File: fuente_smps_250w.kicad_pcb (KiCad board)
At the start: 2 copper layers, 160 x 60 mm, 53 parts, among them J1 Conn_01x03, J2 Conn_01x03, Q1 2N3904, Q2 2N3906, Q3 2N3904, Q4 2N3906, Q5 IRFZ44N, Q6 IRFZ44N, Q7 IRFZ44N, Q8 IRFZ44N, U1 SG3525A, U2 LTV-817S-TA1

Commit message: terminando la  version con sg3525a
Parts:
- moved R13 1.91 mm to (129.6, 70.3)
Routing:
- net Net-(R14-Pad2): track 51.4 -> 63.6 mm, vias 2 -> 0
- net /Filtro/T_B: track 78.8 -> 68.8 mm
- net Net-(D3-Pad2): track 22.7 -> 14.0 mm
- net /OSC_SG3525/VREF: track 62.0 -> 64.9 mm
- net /OSC_SG3525/Sense: track 143.5 -> 141.6 mm
- net /Filtro/T_A: track 72.2 -> 70.8 mm
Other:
- outline, holes or cut-outs redrawn
- board text added: "SG3525A"

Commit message: terminando el diseno
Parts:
- removed the C12 at (195.3, 97.7)
- removed C14: 1000uF, Capacitor_THT:CP_Radial_D10.0mm_P5.00mm
- removed C16: 0.1uF, Capacitor_THT:C_Disc_D3.8mm_W2.6mm_P2.50mm
- removed U2: LTV-817S-TA1, Package_DIP:DIP-4_W7.62mm_LongPads
- added IC1: TL494, Package_DIP:DIP-16_W7.62mm_LongPads, F.Cu at (92.7, 85.2)
- added R15: 270, Resistor_THT:R_Axial_DIN0309_L9.0mm_D3.2mm_P15.24mm_Horizontal, F.Cu at (105.5, 109.0)
- C1: value 15nF -> 2.5uF; footprint Capacitor_THT:C_Disc_D9.0mm_W2.5mm_P5.00mm -> Capacitor_THT:CP_Radial_D4.0mm_P2.00mm
- C13: value 1000uF -> 0.1uF; footprint Capacitor_THT:CP_Radial_D10.0mm_P5.00mm -> Capacitor_THT:C_Disc_D3.8mm_W2.6mm_P2.50mm
- C2: value 0.1uF -> 1nF; footprint Capacitor_THT:C_Disc_D3.8mm_W2.6mm_P2.50mm -> Capacitor_THT:C_Disc_D4.3mm_W1.9mm_P5.00mm
- C3: value 0.1uF -> 0.33uF; footprint Capacitor_THT:C_Disc_D3.8mm_W2.6mm_P2.50mm -> Capacitor_THT:C_Disc_D4.3mm_W1.9mm_P5.00mm
- C4, C5: value 0.1uF -> 1000uF; footprint Capacitor_THT:C_Disc_D3.8mm_W2.6mm_P2.50mm -> Capacitor_THT:CP_Radial_D10.0mm_P5.00mm
- C6: value 0.33uF -> 1000uF; footprint Capacitor_THT:C_Disc_D4.3mm_W1.9mm_P5.00mm -> Capacitor_THT:CP_Radial_D10.0mm_P5.00mm
- D1: value MBRF1080CTR -> D_Zener_ALT; footprint Package_TO_SOT_THT:TO-220-3_Vertical -> Diode_THT:D_A-405_P10.16mm_Horizontal
- D2: value MBRF1080CT -> D_Zener_ALT; footprint Package_TO_SOT_THT:TO-220-3_Vertical -> Diode_THT:D_A-405_P10.16mm_Horizontal
- D3: value D_Zener_ALT -> MBRF1080CTR; footprint Diode_THT:D_A-405_P10.16mm_Horizontal -> Package_TO_SOT_THT:TO-220-3_Vertical
- D4: value D_Zener_ALT -> MBRF1080CT; footprint Diode_THT:D_A-405_P10.16mm_Horizontal -> Package_TO_SOT_THT:TO-220-3_Vertical
- R1: value 4.7K -> 1K
- R10, R9: value 10 -> 1K
- R12: value 270 -> 10; footprint Resistor_THT:R_Axial_DIN0309_L9.0mm_D3.2mm_P15.24mm_Horizontal -> Resistor_THT:R_Axial_DIN0207_L6.3mm_D2.5mm_P10.16mm_Horizontal
- R13: value 1K -> 10
- R14: value 510 -> 10
- R2: value 4.7K -> 510
- R3: value 4.7K -> 9.1K
- R4: value 33 -> 1K
- R5: value 820 -> 510
- R6: value 1K -> 51K
- R7: value 1K -> 50K
- R8: value 10 -> 10K
- U1: value SG3525A -> LTV-817S-TA1; footprint Package_DIP:DIP-16_W7.62mm_LongPads -> Package_DIP:DIP-4_W7.62mm_LongPads
- moved C5 112.2 mm to (195.5, 75.5), turned to 270 degrees
- moved C4 105.1 mm to (195.5, 102.5), turned to 90 degrees
- moved R14 88.9 mm to (92.5, 72.5), turned to 0 degrees
- moved R2 77.0 mm to (179.5, 83.5)
- moved C6 63.7 mm to (184.3, 102.5)
- moved U1 56.9 mm to (151.1, 73.0), turned to 180 degrees
- moved R11 54.1 mm to (125.0, 117.5), turned to 180 degrees
- moved D1 49.0 mm to (178.0, 72.5)
- moved R8 36.2 mm to (104.0, 87.5), turned to 270 degrees
- moved D4 35.8 mm to (175.5, 121.5), turned to 180 degrees
- moved D2 34.2 mm to (176.5, 102.5), turned to 90 degrees
- moved R6 33.8 mm to (79.5, 89.0), turned to 0 degrees
- moved C3 32.5 mm to (123.0, 83.8)
- moved R1 29.6 mm to (130.0, 70.5), turned to 0 degrees
- moved R10 28.0 mm to (107.5, 97.5), turned to 90 degrees
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- renumbered C15 to C12
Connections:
- C1 pad 1: Net-(C1-Pad1) -> VREF
- C1 pad 2: GND -> Net-(C1-Pad2)
- C10 pad 1: GNDREF -> /Filtro/VCC
- C10 pad 2: /Filtro/-VCC -> GNDREF
- C11 pad 1: /Filtro/VCC -> GNDREF
- C11 pad 2: GNDREF -> /Filtro/-VCC
- C13 pad 1: /Filtro/VCC -> GNDREF
- C13 pad 2: GNDREF -> /Filtro/-VCC
- C2 pad 1: /OSC_SG3525/VREF -> Net-(C2-Pad1)
- C3 pad 2: GND -> Net-(C3-Pad2)
- C4 pad 1: GND -> /Filtro/VCC
- C4 pad 2: Net-(C4-Pad2) -> GNDREF
- C5 pad 1: GND -> GNDREF
- C5 pad 2: Net-(C5-Pad2) -> /Filtro/-VCC
- C6 pad 1: Net-(C6-Pad1) -> /Filtro/VCC
- C6 pad 2: Net-(C6-Pad2) -> GNDREF
- C7 pad 1: /Filtro/VCC -> GNDREF
- C7 pad 2: GNDREF -> /Filtro/-VCC
- C8 pad 1: GNDREF -> /Filtro/VCC
- C8 pad 2: /Filtro/-VCC -> GNDREF
- C9 pad 1: /Filtro/VCC -> GNDREF
- C9 pad 2: GNDREF -> /Filtro/-VCC
- D1 pad 1: /Filtro/T_A -> Net-(D1-Pad1)
- D1 pad 2: /Filtro/-VCC -> Net-(D1-Pad2)
- D2 pad 1: /Filtro/T_B -> /Filtro/VCC
- D2 pad 2: /Filtro/VCC -> Net-(D1-Pad1)
- D3 pad 1: Net-(D3-Pad1) -> /Filtro/T_A
- D3 pad 2: Net-(D3-Pad2) -> /Filtro/-VCC
- D4 pad 1: /Filtro/VCC -> /Filtro/T_B
- D4 pad 2: Net-(D3-Pad1) -> /Filtro/VCC
- H1 pad 1: GND -> Net-(H1-Pad1)
- H2 pad 1: GND -> Net-(H2-Pad1)
- H3 pad 1: GNDREF -> Net-(H3-Pad1)
- H4 pad 1: GNDREF -> Net-(H4-Pad1)
- J1 pad 2: /OSC_SG3525/shutdown -> (no net)
- Q6 pad 2: Net-(C6-Pad2) -> Net-(C3-Pad2)
- Q8 pad 2: Net-(C6-Pad2) -> Net-(C3-Pad2)
- R1 pad 1: /OSC_SG3525/VREF -> GND
- R1 pad 2: Net-(R1-Pad2) -> /OSC_TL494/Sense
- R10 pad 1: Net-(Q6-Pad1) -> /transformacion/In_B
- R10 pad 2: Net-(Q3-Pad1) -> GND
- R11 pad 1: Net-(Q8-Pad1) -> Net-(Q7-Pad1)
- R11 pad 2: Net-(Q3-Pad1) -> Net-(Q1-Pad1)
- R12 pad 1: Net-(Q5-Pad2) -> Net-(Q5-Pad1)
- R12 pad 2: Net-(C6-Pad1) -> Net-(Q1-Pad1)
- R13 pad 1: GND -> Net-(Q6-Pad1)
- R13 pad 2: /OSC_SG3525/Sense -> Net-(Q3-Pad1)
- R14 pad 1: /Filtro/-VCC -> Net-(Q8-Pad1)
- R14 pad 2: Net-(R14-Pad2) -> Net-(Q3-Pad1)
- R2 pad 1: GND -> /Filtro/-VCC
- R2 pad 2: Net-(R1-Pad2) -> Net-(R2-Pad2)
- R3 pad 1: Net-(R3-Pad1) -> VREF
- R3 pad 2: GND -> Net-(C1-Pad2)
- R4 pad 1: Net-(R4-Pad1) -> Net-(C1-Pad2)
- R4 pad 2: Net-(C1-Pad1) -> GND
- R5 pad 1: Net-(C5-Pad2) -> Net-(IC1-Pad2)
- R5 pad 2: Net-(R5-Pad2) -> VREF
- R6 pad 1: /transformacion/In_A -> Net-(IC1-Pad2)
- R6 pad 2: GND -> Net-(IC1-Pad3)
- R7 pad 1: /transformacion/In_B -> Net-(IC1-Pad6)
- R8 pad 1: Net-(Q7-Pad1) -> +12V
- R8 pad 2: Net-(Q1-Pad1) -> Net-(IC1-Pad11)
- R9 pad 1: Net-(Q5-Pad1) -> /transformacion/In_A
- R9 pad 2: Net-(Q1-Pad1) -> GND
- RV1 pad 2: Net-(R14-Pad2) -> Net-(R2-Pad2)
- RV1 pad 3: Net-(R14-Pad2) -> Net-(R2-Pad2)
- TR1 pad 1: Net-(C6-Pad2) -> Net-(C3-Pad2)
- U1 pad 1: /OSC_SG3525/Sense -> Net-(D1-Pad2)
- U1 pad 2: Net-(R1-Pad2) -> Net-(RV1-Pad1)
- U1 pad 3: Net-(C3-Pad1) -> /OSC_TL494/Sense
- U1 pad 4: Net-(U1-Pad4) -> (no net)
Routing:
- net /OSC_SG3525/Sense: track 141.6 -> 0.00 mm, vias 2 -> 0
- net GND: track 95.8 -> 0.00 mm
- net Net-(C6-Pad2): track 79.7 -> 0.00 mm
- net VREF: track 0.00 -> 73.0 mm
- net GNDREF: track 139.5 -> 66.9 mm
- net /OSC_TL494/Sense: track 0.00 -> 68.1 mm, vias 0 -> 2
- net /OSC_SG3525/VREF: track 64.9 -> 0.00 mm, vias 2 -> 0
- net Net-(R14-Pad2): track 63.6 -> 0.00 mm
- net +12V: track 83.0 -> 140.6 mm, vias 0 -> 2
- net Net-(C3-Pad2): track 0.00 -> 55.7 mm
- net /OSC_SG3525/shutdown: track 49.6 -> 0.00 mm
- net Net-(R2-Pad2): track 0.00 -> 35.9 mm, vias 0 -> 2
- net Net-(C1-Pad2): track 0.00 -> 26.3 mm
- net Net-(C3-Pad1): track 4.44 -> 30.6 mm
- net Net-(D1-Pad2): track 0.00 -> 26.0 mm
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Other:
- board size 160 x 60 mm -> 156.5 x 60 mm
- board text added: "TL494"
- board text removed: "SG3525A"

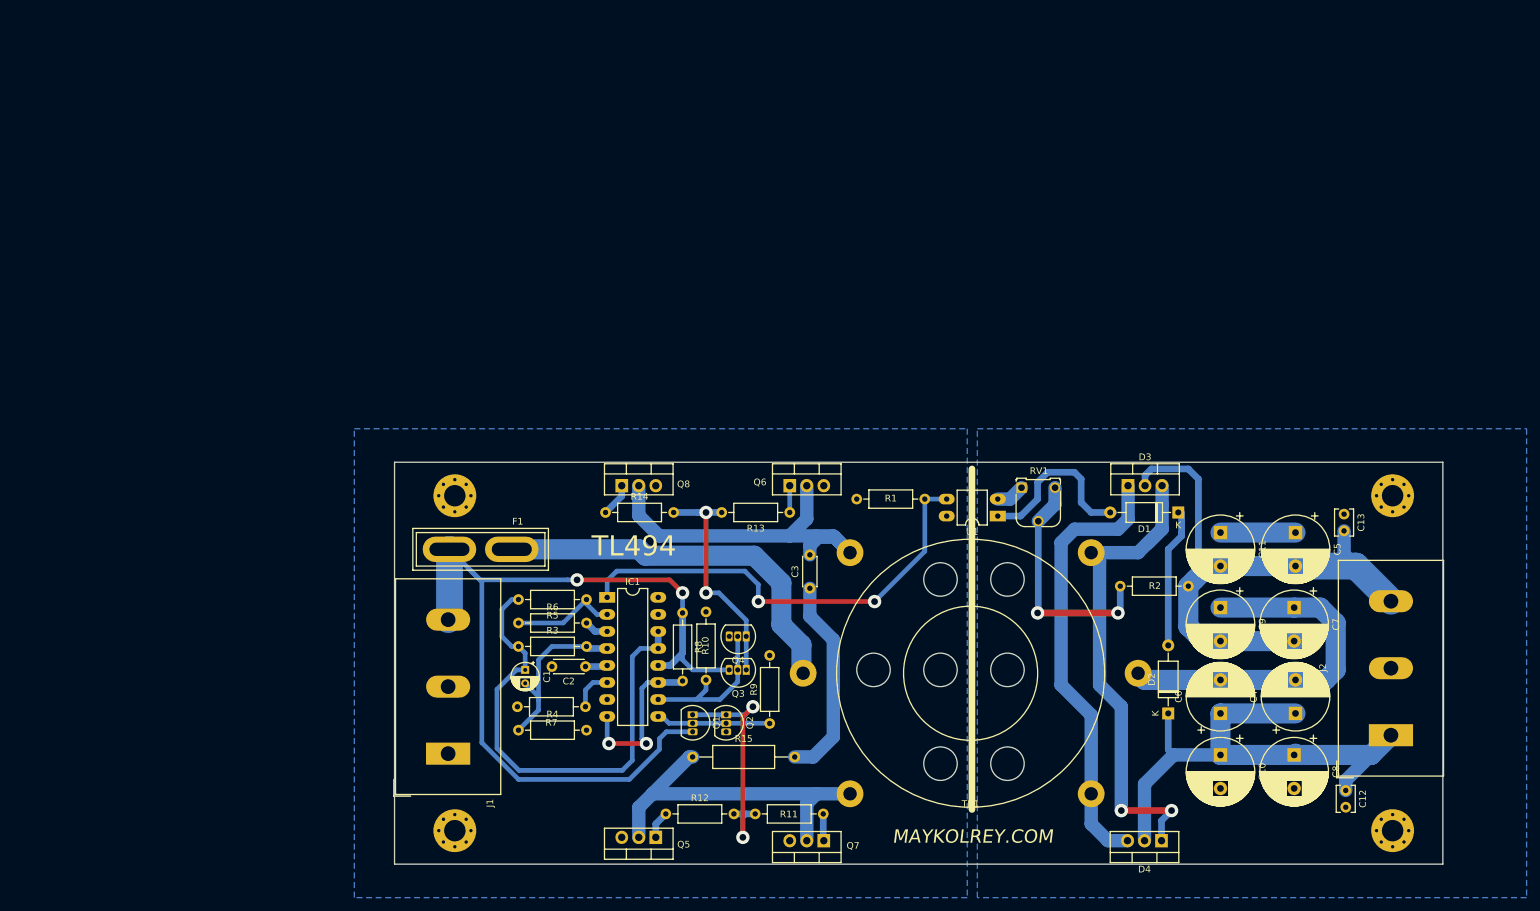
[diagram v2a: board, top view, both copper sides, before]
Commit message: separando el modulo de oscilacion en otra  placa
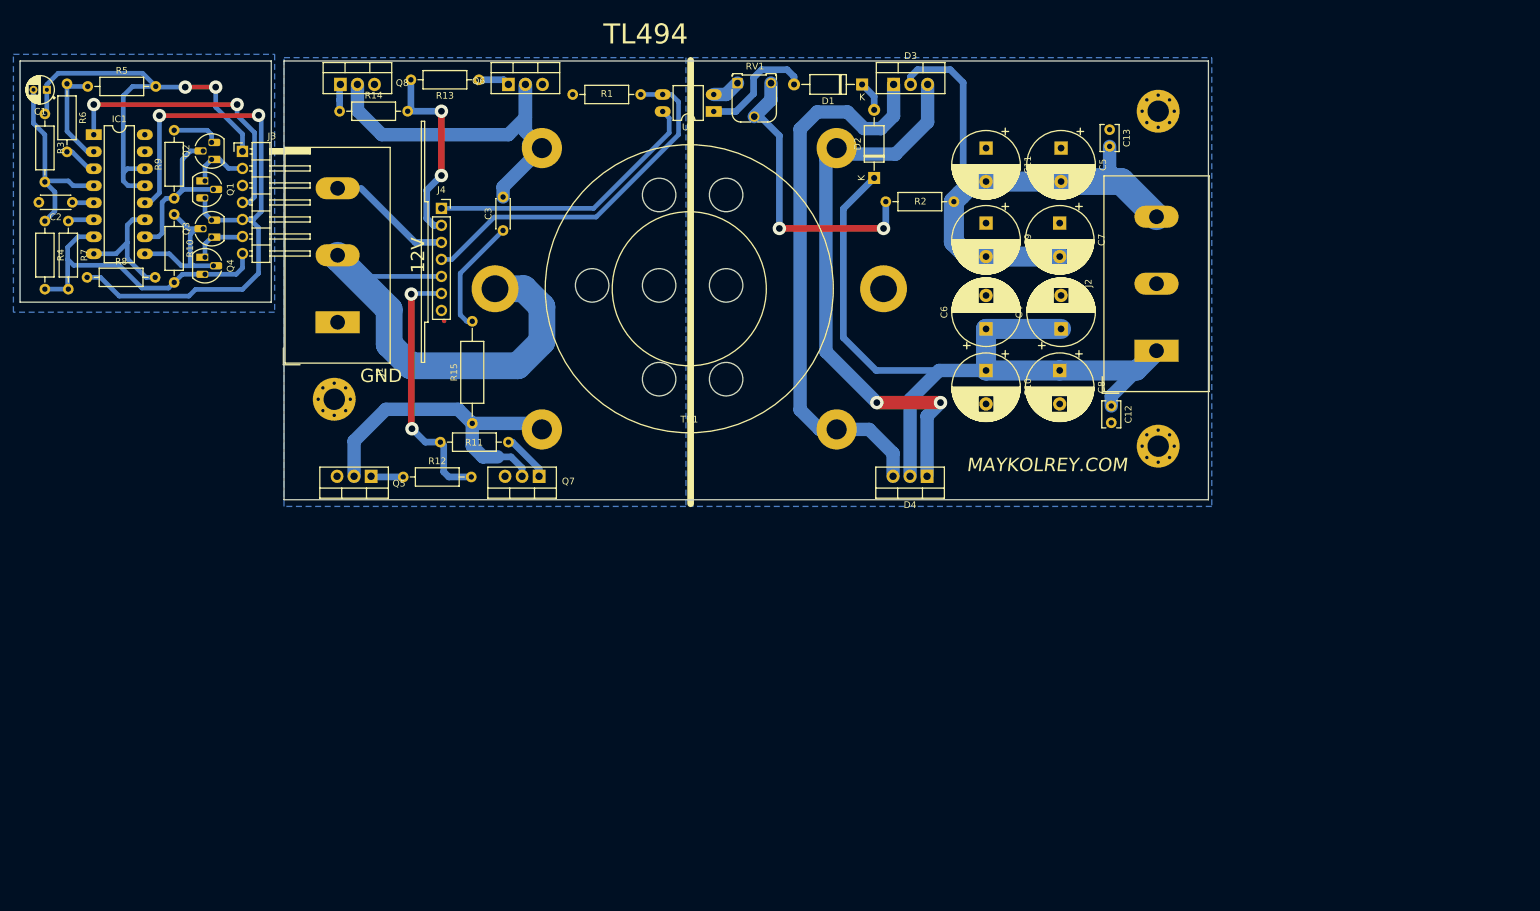
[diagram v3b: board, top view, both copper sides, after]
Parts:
- removed F1: Fuse, Fuse:Fuse_Blade_ATO_directSolder
- removed H2: MountingHole_Pad, MountingHole:MountingHole_3.2mm_M3_Pad_Via
- added J3: Conn_01x03, Connector_PinHeader_2.54mm:PinHeader_1x07_P2.54mm_Horizontal, F.Cu at (38.3, 18.6)
- added J4: Conn_01x03, Connector_PinSocket_2.54mm:PinSocket_1x07_P2.54mm_Vertical, F.Cu at (68.0, 27.1)
- Q1, Q2, Q3, Q4: footprint Package_TO_SOT_THT:TO-92L_Inline -> Package_TO_SOT_THT:TO-92L_HandSolder
- moved R9 118.5 mm to (28.1, 25.6)
- moved Q2 113.0 mm to (33.7, 19.8), turned to 90 degrees
- moved C1 112.2 mm to (9.10, 9.40), turned to 180 degrees
- moved Q1 107.9 mm to (32.7, 23.0)
- moved R5 106.8 mm to (15.2, 8.90), turned to 0 degrees
- moved R3 106.4 mm to (8.80, 13.0), turned to 270 degrees
- moved R7 105.9 mm to (12.3, 29.0), turned to 270 degrees
- moved R10 105.5 mm to (28.1, 28.0), turned to 270 degrees
- moved R6 105.0 mm to (12.1, 8.50), turned to 270 degrees
- moved R4 103.8 mm to (8.80, 29.0), turned to 270 degrees
- moved C2 103.3 mm to (12.9, 26.2)
- moved IC1 103.2 mm to (16.1, 16.1)
- moved Q3 102.7 mm to (33.7, 31.4), turned to 90 degrees
- moved R8 102.0 mm to (15.1, 37.4), turned to 0 degrees
- moved Q4 98.7 mm to (32.7, 34.4), turned to 270 degrees
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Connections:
- net VREF renamed /OSC_TL494/VREF
- C2 pad 2: GND -> GNDA
- IC1 pad 10: /transformacion/In_B -> /OSC_TL494/E2
- IC1 pad 12: +12V -> +12VA
- IC1 pad 7: GND -> GNDA
- IC1 pad 9: /transformacion/In_A -> /OSC_TL494/E1
- J1 pad 2: (no net) -> +12V
- J1 pad 3: +12V -> /shut_in
- Q1 pad 1: Net-(Q1-Pad1) -> /OSC_TL494/Out_B
- Q1 pad 2: /transformacion/In_A -> /OSC_TL494/E2
- Q1 pad 3: +12V -> +12VA
- Q2 pad 1: Net-(Q1-Pad1) -> /OSC_TL494/Out_B
- Q2 pad 2: /transformacion/In_A -> /OSC_TL494/E2
- Q2 pad 3: GND -> GNDA
- Q3 pad 1: Net-(Q3-Pad1) -> /OSC_TL494/Out_A
- Q3 pad 2: /transformacion/In_B -> /OSC_TL494/E1
- Q3 pad 3: +12V -> +12VA
- Q4 pad 1: Net-(Q3-Pad1) -> /OSC_TL494/Out_A
- Q4 pad 2: /transformacion/In_B -> /OSC_TL494/E1
- Q4 pad 3: GND -> GNDA
- R1 pad 2: /OSC_TL494/Sense -> /sense_in
- R10 pad 1: /transformacion/In_B -> /OSC_TL494/E1
- R10 pad 2: GND -> GNDA
- R11 pad 2: Net-(Q1-Pad1) -> /transformacion/In_A
- R12 pad 2: Net-(Q1-Pad1) -> /transformacion/In_A
- R13 pad 2: Net-(Q3-Pad1) -> /transformacion/In_B
- R14 pad 2: Net-(Q3-Pad1) -> /transformacion/In_B
- R4 pad 2: GND -> GNDA
- R7 pad 2: GND -> GNDA
- R8 pad 1: +12V -> +12VA
- R9 pad 1: /transformacion/In_A -> /OSC_TL494/E2
- R9 pad 2: GND -> GNDA
- TR1 pad 2: Net-(F1-Pad1) -> +12V
- U1 pad 3: /OSC_TL494/Sense -> /sense_in
- U1 pad 4: (no net) -> /vref_in
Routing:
- net +12VA: track 0.00 -> 93.3 mm, vias 0 -> 2
- net +12V: track 140.6 -> 72.2 mm, vias 2 -> 0
- net GNDREF: track 66.9 -> 1.41 mm
- net Net-(F1-Pad1): track 57.2 -> 0.00 mm
- net /sense_in: track 0.00 -> 54.1 mm
- net GNDA: track 0.00 -> 52.5 mm
- net /Filtro/VCC: track 83.5 -> 128.8 mm
- net /vref_in: track 0.00 -> 42.3 mm
- net Net-(Q1-Pad1): track 36.5 -> 0.00 mm, vias 2 -> 0
- net Net-(Q3-Pad1): track 35.4 -> 0.00 mm, vias 2 -> 0
- net /OSC_TL494/E2: track 0.00 -> 26.2 mm
- net /OSC_TL494/Sense: track 68.1 -> 42.9 mm
- net /OSC_TL494/E1: track 0.00 -> 23.5 mm
- net /transformacion/In_A: track 17.1 -> 38.8 mm, vias 0 -> 2
- net /shut_in: track 0.00 -> 17.8 mm
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- added copper zone on B.Cu, net GNDA
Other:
- board size 156.5 x 60 mm -> 177.4 x 65.5 mm
- board text added: "12V"
- board text added: "GND"
